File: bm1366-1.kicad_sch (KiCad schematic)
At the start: 61 parts, among them U1 25MHz, U13 ADP171AUJ-R7, U14 BM1366_mode1, U23 ADP171AUJ-R7

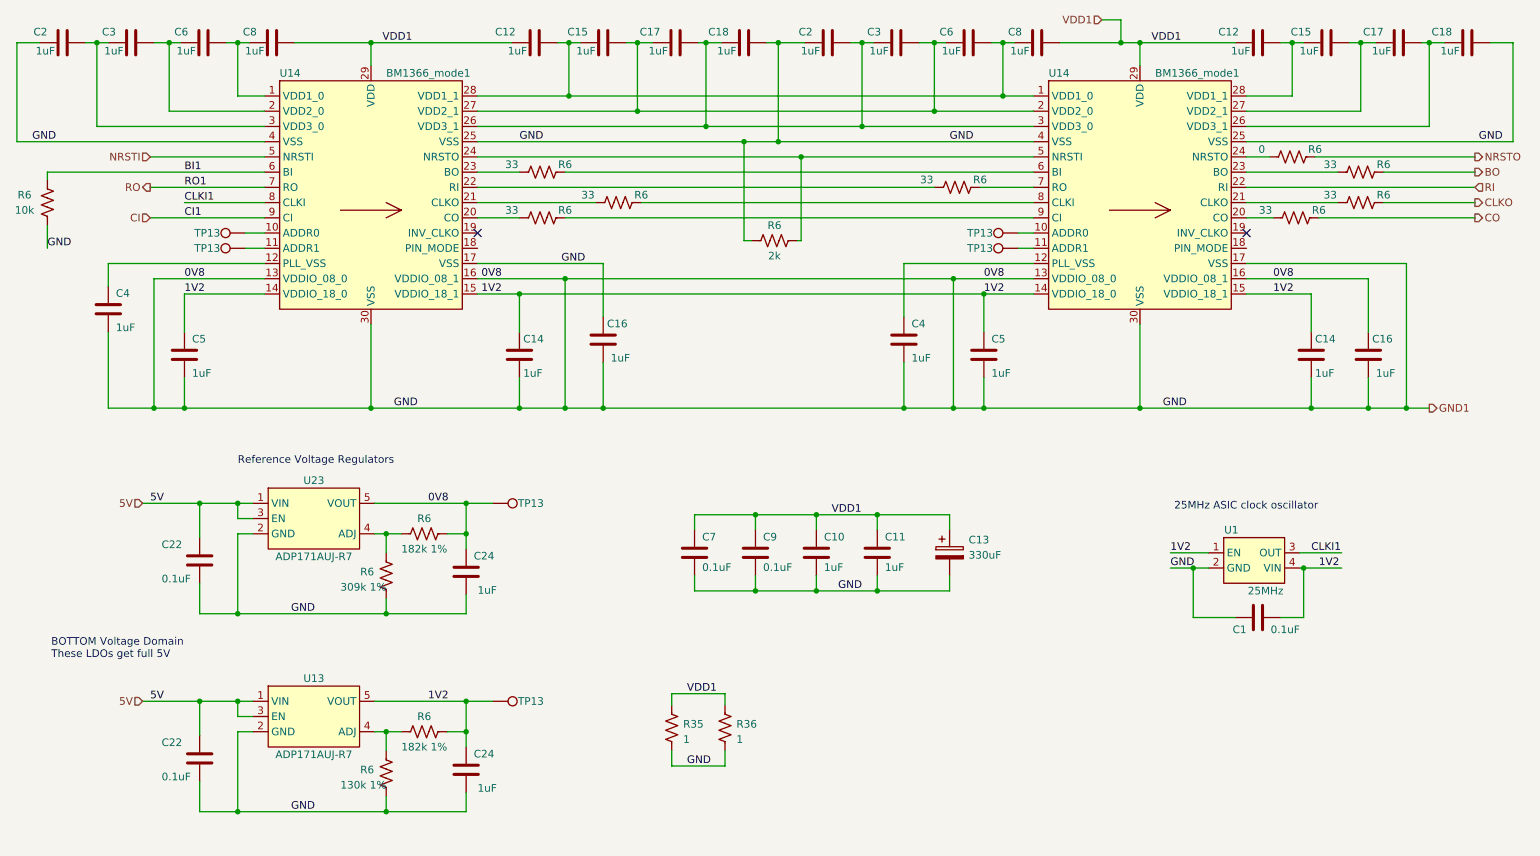
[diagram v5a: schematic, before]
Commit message: routed 1366 changes
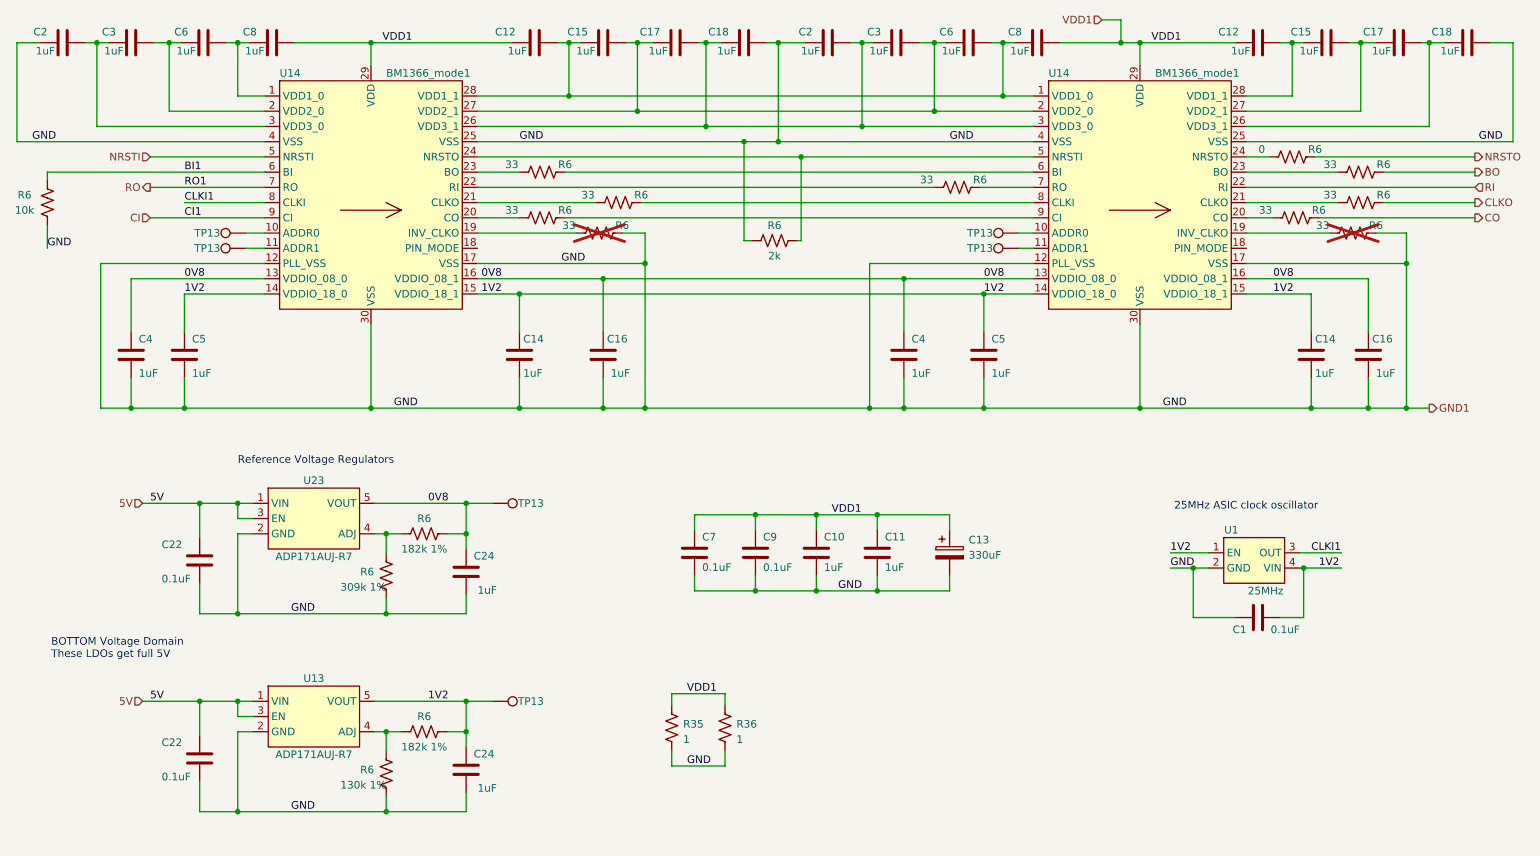
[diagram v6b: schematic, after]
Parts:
- added R6 (x2): 33, Resistor_SMD:R_0402_1005Metric, symbol Device:R_US
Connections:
- net GND1: now also U14.12 (PLL_VSS), U14.12 (PLL_VSS), R6.2, R6.2; no longer C16.1, C16.1, C24.1, R6.1, TP13.1, U14.13 (VDDIO_08_0), U14.13 (VDDIO_08_0), U14.16 (VDDIO_08_1), U14.16 (VDDIO_08_1), U23.5 (VOUT)
- net 0V8: now reaches C4.1
- net 0V8: now also C16.1, C16.1, C24.1, C4.1, R6.1, TP13.1, U14.13 (VDDIO_08_0), U14.13 (VDDIO_08_0), U14.16 (VDDIO_08_1), U14.16 (VDDIO_08_1), U23.5 (VOUT); no longer U14.12 (PLL_VSS)
- net at U14.19 (INV_CLKO): now also R6.1 (x2)
- no-connect marks 2 -> 0
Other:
- moved on the sheet: C16, C4

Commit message: Fix some part numbers in the BOM
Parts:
- R35, R36: DK 311-1.00LRCT-ND -> 118-CR2512-F/-1R00ELFCT-ND; PARTNO RC0402FR-071RL -> CR2512-F/-1R00ELF
- R6: DK (none) -> YAG2303CT-ND; PARTNO (none) -> RT0402BRD072KL
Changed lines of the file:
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@@
+      (effects (font (size 1.27 1.27)) hide)
+    )
+    (property "DK" "YAG2303CT-ND" (at 139.7 99.06 90)
+      (effects (font (size 1.27 1.27)) hide)
+    )
+    (property "PARTNO" "RT0402BRD072KL" (at 139.7 99.06 90)
       (effects (font (size 1.27 1.27)) hide)
     )
@@
       (effects (font (size 1.27 1.27)) hide)
     )
-    (property "DK" "311-1.00LRCT-ND" (at 131.445 180.34 0)
-      (effects (font (size 1.27 1.27)) hide)
-    )
-    (property "PARTNO" "RC0402FR-071RL" (at 131.445 180.34 0)
+    (property "DK" "118-CR2512-F/-1R00ELFCT-ND" (at 131.445 180.34 0)
+      (effects (font (size 1.27 1.27)) hide)
+    )
+    (property "PARTNO" "CR2512-F/-1R00ELF" (at 131.445 180.34 0)
       (effects (font (size 1.27 1.27)) hide)
     )
@@
       (effects (font (size 1.27 1.27)) hide)
     )
-    (property "DK" "311-1.00LRCT-ND" (at 122.555 180.34 0)
-      (effects (font (size 1.27 1.27)) hide)
-    )
-    (property "PARTNO" "RC0402FR-071RL" (at 122.555 180.34 0)
-      (effects (font (size 1.27 1.27)) hide)
-    )
+    (property "DK" "118-CR2512-F/-1R00ELFCT-ND" (at 122.555 180.34 0)
+      (effects (font (size 1.27 1.27)) hide)
+    )
+    (property "PARTNO" "CR2512-F/-1R00ELF" (at 122.555 180.34 0)
+      (effects (font (size 1.27 1.27)) hide)
+    )

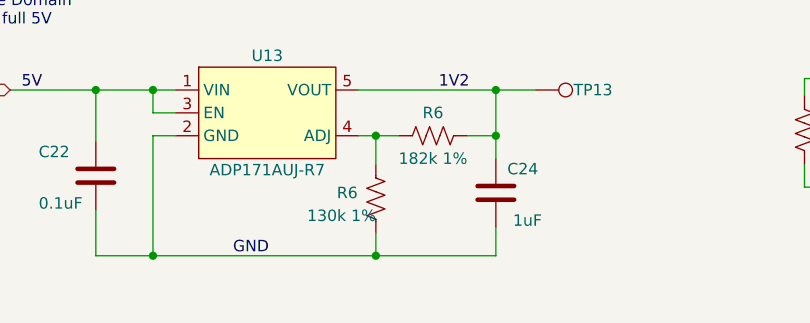
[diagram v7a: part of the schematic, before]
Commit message: add option for 1.5V ASIC Vref
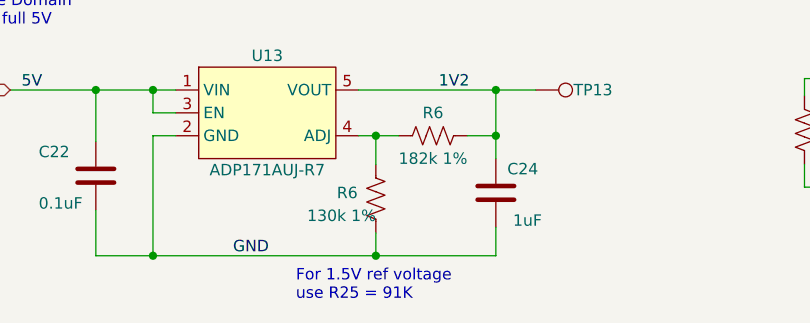
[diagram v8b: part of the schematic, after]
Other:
- note added: "For 1.5V ref voltage use R25 = 91K"
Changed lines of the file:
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@@
+    (effects (font (size 1.27 1.27)) (justify left bottom))
+  )
+  (text "For 1.5V ref voltage\nuse R25 = 91K" (at 66.04 199.39 0)
     (effects (font (size 1.27 1.27)) (justify left bottom))
   )
